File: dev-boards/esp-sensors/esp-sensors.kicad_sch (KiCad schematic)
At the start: 24 parts, among them J0 JST XH/PH, J1 JST SH, J2 JST SH, J3 JST SH, J4 JST SH, J5 JST SH, Q1 2N7002DW, Q2 BSS138, U5 TEMT6000X01

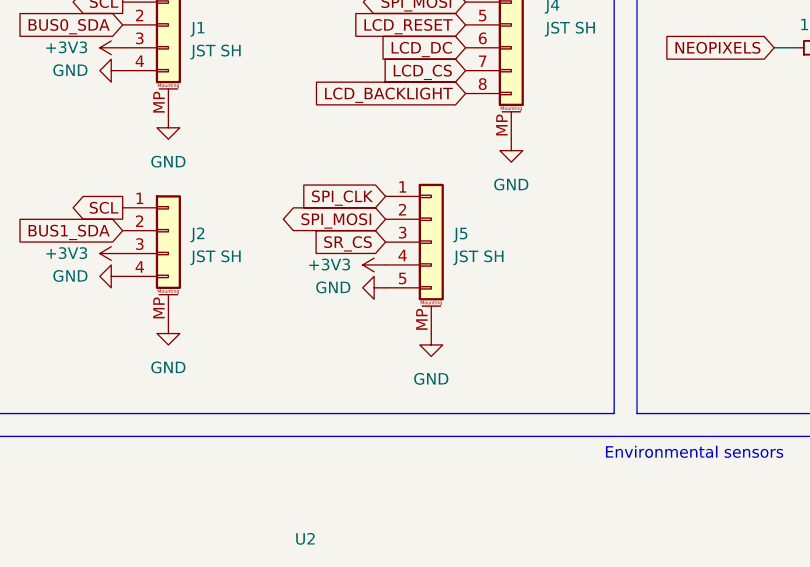
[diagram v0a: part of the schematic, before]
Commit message: Tweak pinout for SR connector on esp-sensors
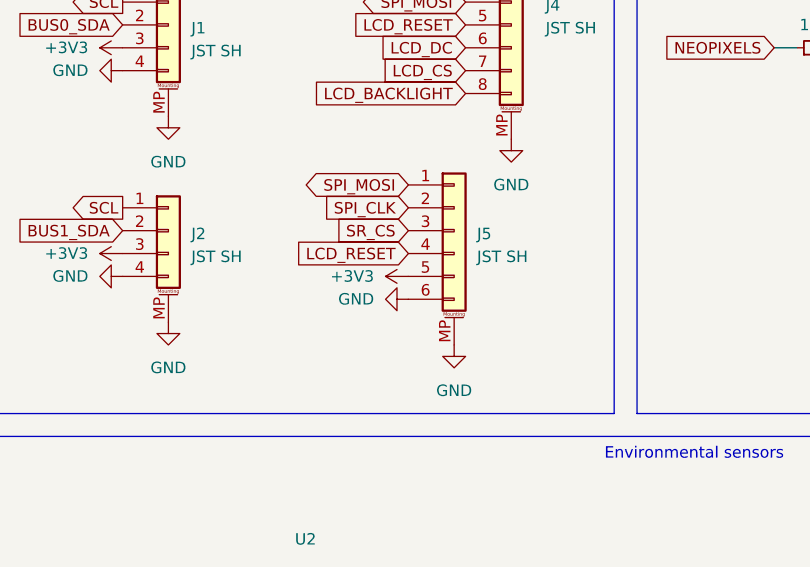
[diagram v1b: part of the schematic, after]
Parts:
- removed J5: JST SH, custom:JST_SH_SM05B-SRSS-TB_1x05-1MP_P1.00mm_Horizontal, symbol Connector_Generic_MountingPin:Conn_01x05_MountingPin
- added J5: JST SH, custom:JST_SH_SM06B-SRSS-TB_1x06-1MP_P1.00mm_Horizontal, symbol Connector_Generic_MountingPin:Conn_01x06_MountingPin
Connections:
- net +3V3: now also J5.5 (Pin_5)
- net GND: now also J5.6 (Pin_6), J5.MP (MountPin)
- net LCD_RESET: now also J5.4 (Pin_4)
- net SPI_CLK: now also J5.2 (Pin_2)
- net SPI_MOSI: now also J5.1 (Pin_1)
- net SR_CS: now also J5.3 (Pin_3)
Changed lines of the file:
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@@
 	(global_label "SR_CS"
 		(shape input)
-		(at 166.37 52.07 180)
+		(at 168.91 50.8 180)
 		(fields_autoplaced yes)
 		(effects
@@
 		)
 		(property "Intersheetrefs" "${INTERSHEET_REFS}"
-			(at 159.8772 52.07 0)
+			(at 162.4172 50.8 0)
 			(effects
 				(font
@@
 	(global_label "SPI_MOSI"
 		(shape bidirectional)
-		(at 166.37 49.53 180)
+		(at 168.91 45.72 180)
 		(fields_autoplaced yes)
 		(effects
@@
 		)
 		(property "Intersheetrefs" "${INTERSHEET_REFS}"
-			(at 157.6773 49.53 0)
+			(at 160.2173 45.72 0)
 			(effects
 				(font
@@
 	(global_label "SPI_CLK"
 		(shape input)
-		(at 166.37 46.99 180)
+		(at 168.91 48.26 180)
 		(fields_autoplaced yes)
 		(effects
@@
 		)
 		(property "Intersheetrefs" "${INTERSHEET_REFS}"
-			(at 159.8167 46.99 0)
+			(at 162.3567 48.26 0)
 			(effects
 				(font
@@
 		)
 	)
+	(global_label "LCD_RESET"
+		(shape input)
+		(at 168.91 53.34 180)
+		(fields_autoplaced yes)
+		(effects
+			(font
+				(size 1.27 1.27)
+			)
+			(justify right)
+		)
+		(property "Intersheetrefs" "${INTERSHEET_REFS}"
+			(at 155.644 53.34 0)
+			(effects
+				(font
+					(size 1.27 1.27)
+				)
+				(justify right)
+				(hide yes)
+			)
+		)
+	)
 	(global_label "SCL"
 		(shape output)
@@
 	)
 	(symbol
+		(lib_id "power:GND")
+		(at 173.99 63.5 0)
+		(unit 1)
+		(exclude_from_sim no)
+		(in_bom yes)
+		(on_board yes)
+		(dnp no)
+		(fields_autoplaced yes)
+		(property "Reference" "#PWR036"
+			(at 173.99 69.85 0)
+			(effects
+				(font
+					(size 1.27 1.27)
+				)
+				(hide yes)
+			)
+		)
+		(property "Value" "GND"
+			(at 173.99 68.58 0)
+			(effects
+				(font
+					(size 1.27 1.27)
+				)
+			)
+		)
+		(property "Footprint" ""
+			(at 173.99 63.5 0)
+			(effects
+				(font
+					(size 1.27 1.27)
+				)
+				(hide yes)
+			)
+		)
+		(property "Datasheet" ""
+			(at 173.99 63.5 0)
+			(effects
+				(font
+					(size 1.27 1.27)
+				)
+				(hide yes)
+			)
+		)
+		(property "Description" "Power symbol creates a global label with name \"GND\" , ground"
+			(at 173.99 63.5 0)
+			(effects
+				(font
+					(size 1.27 1.27)
+				)
+				(hide yes)
+			)
+		)
+		(pin "1"
+		)
+		(instances
+			(project "esp-sensors"
+				(path "/76a56607-25e2-40a3-9282-ff279b153f75"
+					(reference "#PWR036")
+					(unit 1)
+				)
+			)
+		)
+	)
+	(symbol
 		(lib_id "aliexpress:ENS160+AHT2x")
 		(at 157.48 123.19 0)
@@
 	)
 	(symbol
-		(lib_id "power:GND")
-		(at 171.45 62.23 0)
-		(unit 1)
-		(exclude_from_sim no)
-		(in_bom yes)
-		(on_board yes)
-		(dnp no)
-		(fields_autoplaced yes)
-		(property "Reference" "#PWR036"
-			(at 171.45 68.58 0)
-			(effects
-				(font
-					(size 1.27 1.27)
-				)
-				(hide yes)
-			)
-		)
-		(property "Value" "GND"
-			(at 171.45 67.31 0)
-			(effects
-				(font
-					(size 1.27 1.27)
-				)
-			)
-		)
-		(property "Footprint" ""
-			(at 171.45 62.23 0)
-			(effects
-				(font
-					(size 1.27 1.27)
-				)
-				(hide yes)
-			)
-		)
-		(property "Datasheet" ""
-			(at 171.45 62.23 0)
-			(effects
-				(font
-					(size 1.27 1.27)
-				)
-				(hide yes)
-			)
-		)
-		(property "Description" "Power symbol creates a global label with name \"GND\" , ground"
-			(at 171.45 62.23 0)
-			(effects
-				(font
-					(size 1.27 1.27)
-				)
-				(hide yes)
-			)
-		)
-		(pin "1"
-		)
-		(instances
-			(project "esp-sensors"
-				(path "/76a56607-25e2-40a3-9282-ff279b153f75"
-					(reference "#PWR036")
-					(unit 1)
-				)
-			)
-		)
-	)
-	(symbol
 		(lib_id "Device:R_Small")
 		(at 208.28 124.46 0)
@@
 	)
 	(symbol
-		(lib_id "Connector_Generic_MountingPin:Conn_01x05_MountingPin")
-		(at 171.45 52.07 0)
-		(unit 1)
-		(exclude_from_sim no)
-		(in_bom yes)
-		(on_board yes)
-		(dnp no)
-		(fields_autoplaced yes)
-		(property "Reference" "J5"
-			(at 173.99 51.1555 0)
-			(effects
-				(font
-					(size 1.27 1.27)
-				)
-				(justify left)
-			)
-		)
-		(property "Value" "JST SH"
-			(at 173.99 53.6955 0)
-			(effects
-				(font
-					(size 1.27 1.27)
-				)
-				(justify left)
-			)
-		)
-		(property "Footprint" "custom:JST_SH_SM05B-SRSS-TB_1x05-1MP_P1.00mm_Horizontal"
-			(at 171.45 52.07 0)
-			(effects
-				(font
-					(size 1.27 1.27)
-				)
-				(hide yes)
-			)
-		)
-		(property "Datasheet" "~"
-			(at 171.45 52.07 0)
-			(effects
-				(font
-					(size 1.27 1.27)
-				)
-				(hide yes)
-			)
-		)
-		(property "Description" "Generic connectable mounting pin connector, single row, 01x05, script generated (kicad-library-utils/schlib/autogen/connector/)"
-			(at 171.45 52.07 0)
-			(effects
-				(font
-					(size 1.27 1.27)
-				)
-				(hide yes)
-			)
-		)
-		(pin "5"
-		)
-		(pin "2"
-		)
-		(pin "1"
-		)
-		(pin "MP"
-		)
-		(pin "4"
-		)
-		(pin "3"
-		)
-		(instances
-			(project ""
-				(path "/76a56607-25e2-40a3-9282-ff279b153f75"
-					(reference "J5")
-					(unit 1)
-				)
-			)
-		)
-	)
-	(symbol
 		(lib_id "power:+3V3")
 		(at 97.79 91.44 0)
@@
 	(symbol
 		(lib_id "power:GND")
-		(at 166.37 57.15 270)
+		(at 168.91 58.42 270)
 		(unit 1)
 		(exclude_from_sim no)
@@
 		(fields_autoplaced yes)
 		(property "Reference" "#PWR035"
-			(at 160.02 57.15 0)
+			(at 162.56 58.42 0)
 			(effects
 				(font
@@
 		)
 		(property "Value" "GND"
-			(at 162.56 57.1499 90)
+			(at 165.1 58.4199 90)
 			(effects
 				(font
@@
 		)
 		(property "Footprint" ""
-			(at 166.37 57.15 0)
+			(at 168.91 58.42 0)
 			(effects
 				(font
@@
 		)
 		(property "Datasheet" ""
-			(at 166.37 57.15 0)
+			(at 168.91 58.42 0)
 			(effects
 				(font
@@
 		)
 		(property "Description" "Power symbol creates a global label with name \"GND\" , ground"
-			(at 166.37 57.15 0)
+			(at 168.91 58.42 0)
 			(effects
 				(font
@@
 	(symbol
 		(lib_id "power:+3V3")
-		(at 166.37 54.61 90)
+		(at 168.91 55.88 90)
 		(unit 1)
 		(exclude_from_sim no)
@@
 		(fields_autoplaced yes)
 		(property "Reference" "#PWR034"
-			(at 170.18 54.61 0)
+			(at 172.72 55.88 0)
 			(effects
 				(font
@@
 		)
 		(property "Value" "+3V3"
-			(at 162.56 54.6099 90)
+			(at 165.1 55.8799 90)
 			(effects
 				(font
@@
 		)
 		(property "Footprint" ""
-			(at 166.37 54.61 0)
+			(at 168.91 55.88 0)
 			(effects
 				(font
@@
 		)
 		(property "Datasheet" ""
-			(at 166.37 54.61 0)
+			(at 168.91 55.88 0)
 			(effects
 				(font
@@
 		)
 		(property "Description" "Power symbol creates a global label with name \"+3V3\""
-			(at 166.37 54.61 0)
+			(at 168.91 55.88 0)
 			(effects
 				(font
@@
 					(unit 1)
 				)
+			)
+		)
+	)
+	(symbol
+		(lib_id "Connector_Generic_MountingPin:Conn_01x06_MountingPin")
+		(at 173.99 50.8 0)
+		(unit 1)
+		(exclude_from_sim no)
+		(in_bom yes)
+		(on_board yes)
+		(dnp no)
+		(fields_autoplaced yes)
+		(property "Reference" "J5"
+			(at 176.53 51.1555 0)
+			(effects
+				(font
+					(size 1.27 1.27)
+				)
+				(justify left)
+			)
+		)
+		(property "Value" "JST SH"
+			(at 176.53 53.6955 0)
+			(effects
+				(font
+					(size 1.27 1.27)
+				)
+				(justify left)
+			)
+		)
+		(property "Footprint" "custom:JST_SH_SM06B-SRSS-TB_1x06-1MP_P1.00mm_Horizontal"
+			(at 173.99 50.8 0)
+			(effects
+				(font
+					(size 1.27 1.27)
+				)
+				(hide yes)
+			)
+		)
+		(property "Datasheet" "~"
+			(at 173.99 50.8 0)
+			(effects
+				(font
+					(size 1.27 1.27)
+				)
+				(hide yes)
+			)
+		)
+		(property "Description" "Generic connectable mounting pin connector, single row, 01x06, script generated (kicad-library-utils/schlib/autogen/connector/)"
+			(at 173.99 50.8 0)
+			(effects
+				(font
+					(size 1.27 1.27)
+				)
+				(hide yes)
+			)
+		)
+		(pin "6"
+		)
+		(pin "5"
+		)
+		(pin "3"
+		)
+		(pin "4"
+		)
+		(pin "1"
+		)
+		(pin "2"
+		)
+		(pin "MP"
+		)
+		(instances
+			(project ""
+				(path "/76a56607-25e2-40a3-9282-ff279b153f75"
+					(reference "J5")
+					(unit 1)
+				)
